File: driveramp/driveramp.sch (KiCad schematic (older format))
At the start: 90 parts, among them J1 SMA, J2 SMA, K1 CONN_3, K2 CONN_3, P2 CONN_2, Q1 BC547BTA, T1 MABACT0067, T2 2x Fair-Rite 2843006802, coax, U1 DG9411, U2 MRFE6VP100H, U3 LM317HV, U4 7321MF, U5 LT3010EMS8E

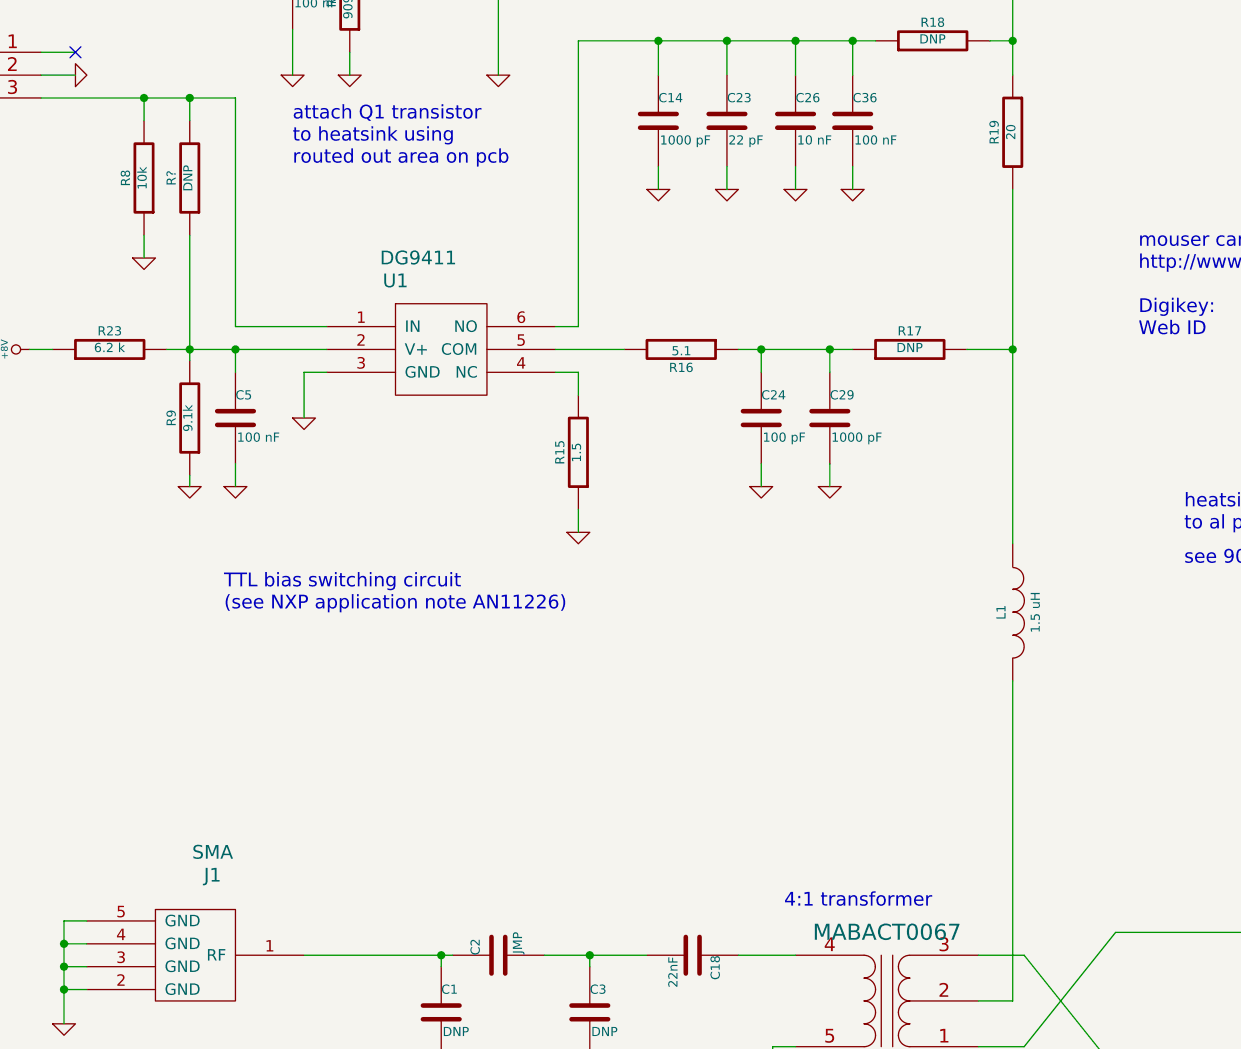
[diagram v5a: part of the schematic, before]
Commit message: added missing cap on rf gnd of input transformer-balun..
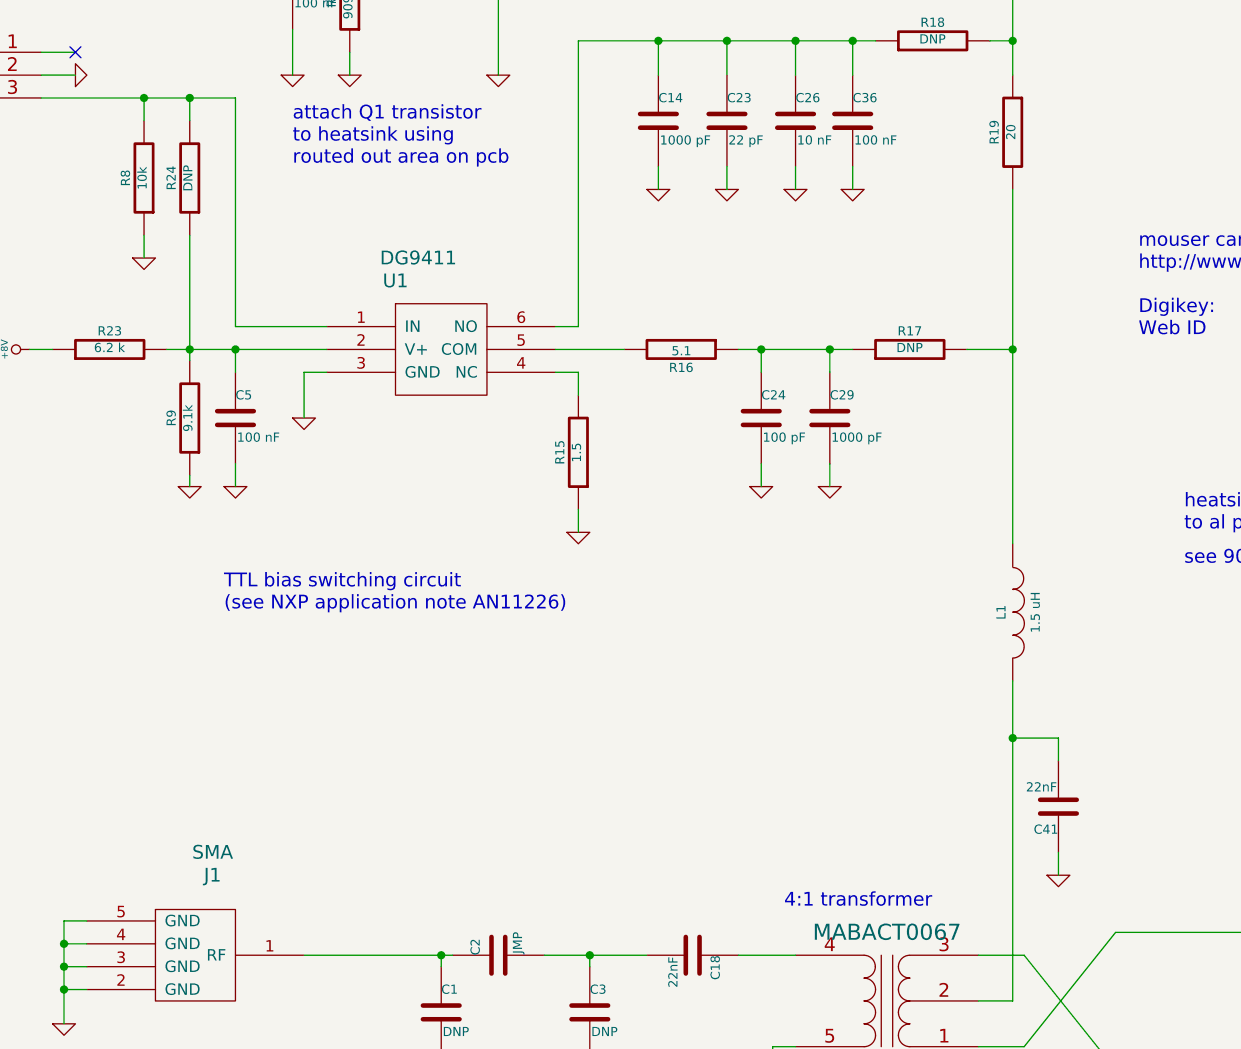
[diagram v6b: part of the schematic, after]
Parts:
- added C41: 22nF, SMD_Packages:SMD-0805, symbol C
- gave numbers to parts that had none: 1
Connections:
- net GND: now also C41.1
- net at L1.2, T1.2 (PM): now also C41.2

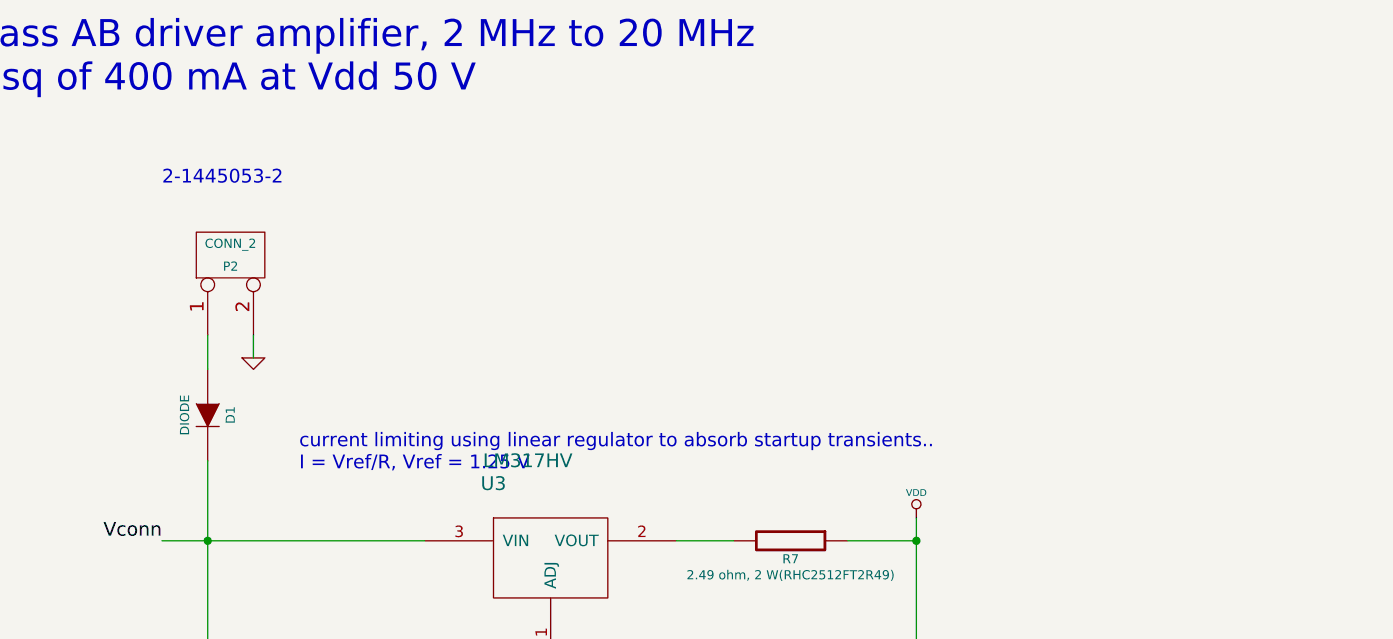
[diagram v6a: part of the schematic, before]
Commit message: moved amp from control board to rxfe
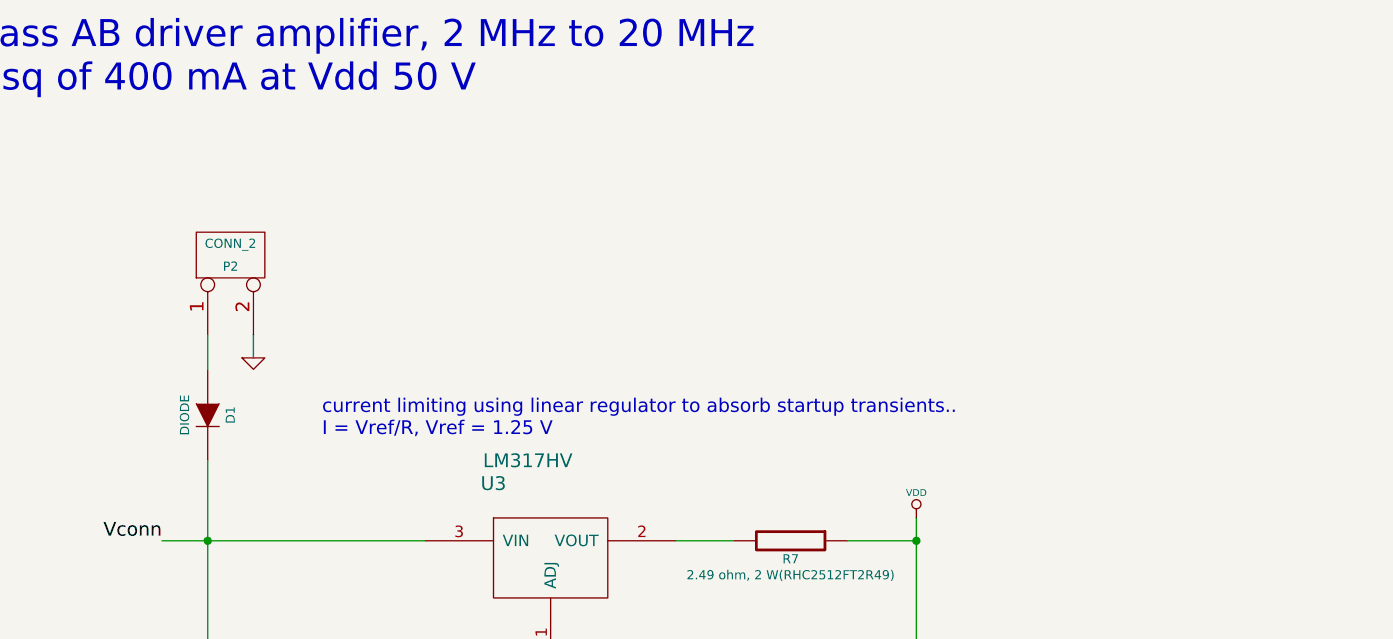
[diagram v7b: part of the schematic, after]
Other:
- note removed: "2-1445053-2"
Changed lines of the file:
@@
 Text Notes 5950 5050 0    60   ~ 0
 mouser cart:\nhttp://www.mouser.com/ProjectManager/ProjectDetail.aspx?AccessID=78a24cbee4\n\nDigikey: \nWeb ID	  	106262028	   	Access ID	  	70481
-Text Notes 11750 1500 0    60   ~ 0
-2-1445053-2
 $Comp
 L GND #PWR57
@@
 	0    1    1    0
 $EndComp
-Text Notes 12350 2750 0    60   ~ 0
+Text Notes 12450 2600 0    60   ~ 0
 current limiting using linear regulator to absorb startup transients..\nI = Vref/R, Vref = 1.25 V
 Text Notes 6050 950  0    118  ~ 0

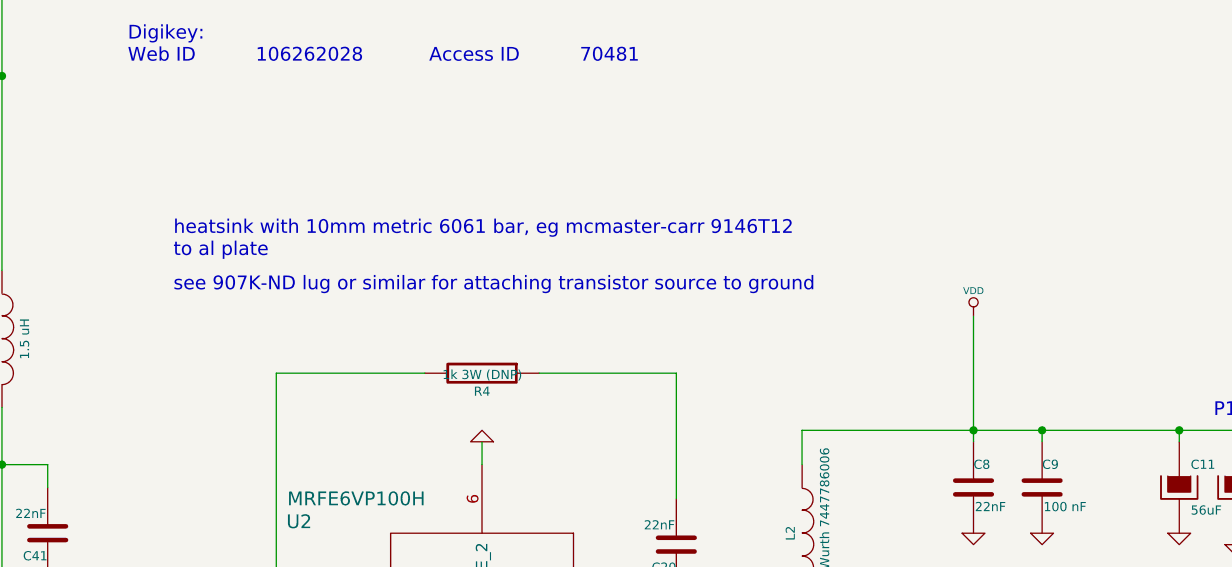
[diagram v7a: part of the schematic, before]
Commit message: added mounting holes for driver amp transistor, removed temp files from git
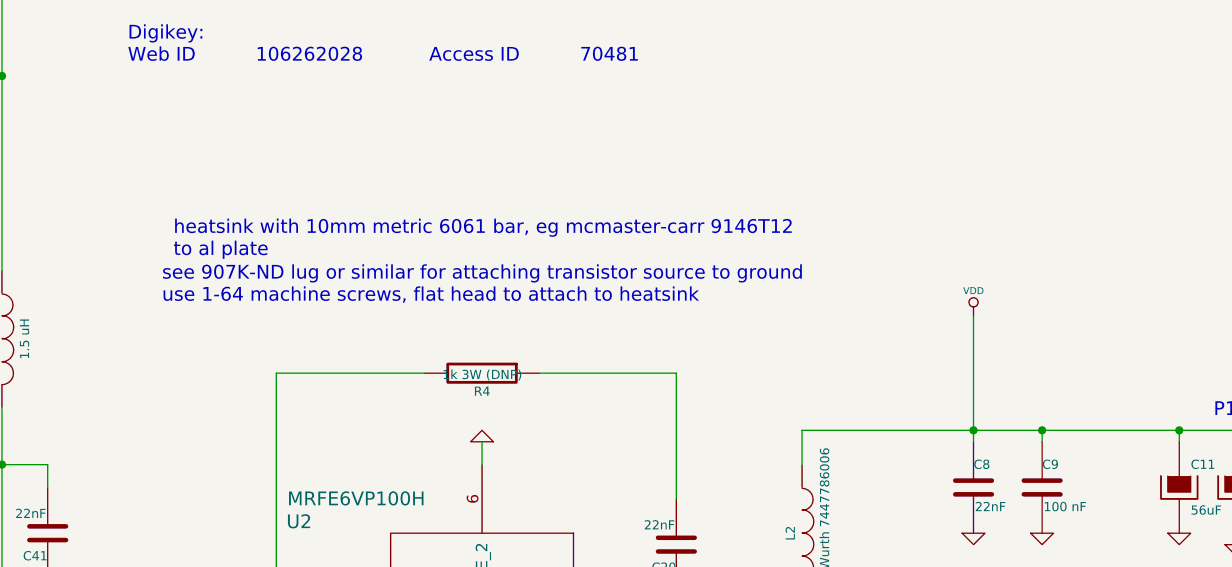
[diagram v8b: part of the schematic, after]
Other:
- note added: "see 907K-ND lug or similar for attaching transistor source to ground\nuse 1-64 machine screws, flat head to attach to heatsink\n"
- note removed: "see 907K-ND lug or similar for attaching transistor source to ground"
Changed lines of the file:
@@
 	1    0    0    -1
 $EndComp
-Text Notes 6150 6050 0    60   ~ 0
-see 907K-ND lug or similar for attaching transistor source to ground
+Text Notes 6100 6100 0    60   ~ 0
+see 907K-ND lug or similar for attaching transistor source to ground\nuse 1-64 machine screws, flat head to attach to heatsink\n
 $Comp
 L 7321MF U4
